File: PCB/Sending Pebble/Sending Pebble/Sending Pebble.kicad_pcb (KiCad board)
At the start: 4 copper layers, 50 x 72 mm, 46 parts, among them J1 USB_C_Receptacle_USB2.0_16P, J2 Conn_01x02_Socket, J3 u.Fl, J4 SMA, J5 Conn_01x02_Socket, Q1 IRLML0030, SW1 Boot, SW2 Reset, U1 LoRa-E5, U3 MAX-M10S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

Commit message: Power Circuitry almost finished
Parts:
- added R15: 10k, Resistor_SMD:R_0603_1608Metric, F.Cu at (28.8, 62.7)
- added R16: 36k, Resistor_SMD:R_0603_1608Metric, F.Cu at (28.8, 65.2)
- R10: value 3k -> 1.27k
- R9: value 3k -> 1.1k
- moved C3 112.0 mm to (133.6, 96.1)
- moved R8 105.4 mm to (137.8, 96.7), turned to 90 degrees
- moved R7 105.1 mm to (136.2, 96.7), turned to 90 degrees
- moved R9 97.4 mm to (132.2, 92.5), turned to -90 degrees
- moved R3 96.7 mm to (124.9, 88.9), turned to 180 degrees
- moved R10 96.0 mm to (125.7, 92.4)
- moved R2 95.8 mm to (125.7, 94.0), turned to 180 degrees
- moved U5 83.2 mm to (136.9, 89.9), turned to 90 degrees
- moved J5 71.6 mm to (144.4, 93.1), turned to 180 degrees
- moved U7 70.2 mm to (129.5, 95.3)
- moved J2 70.2 mm to (121.2, 98.8)
- moved R11 54.6 mm to (70.7, 87.8)
- moved R12 50.7 mm to (66.2, 87.9)
- moved D2 47.7 mm to (120.7, 82.0), turned to 180 degrees
- moved C11 22.8 mm to (61.9, 35.4)
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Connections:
- C3 pad 1: VBAT -> Net-(J5-Pin_2)
- C4 pad 1: Net-(J5-Pin_1) -> +3.3V
- J2 pad 1: Net-(J2-Pin_1) -> GND
- J2 pad 2: GND -> Net-(J2-Pin_2)
- J5 pad 1: Net-(J5-Pin_1) -> VBAT
- J5 pad 2: +3.3V -> Net-(J5-Pin_2)
- R10 pad 1: unconnected-(R10-Pad1) -> GND
- R9 pad 1: unconnected-(R9-Pad1) -> GND
- U1 pad 26: unconnected-(U1-PB14-Pad26) -> ADC
- U5 pad 1: VBAT -> Net-(J5-Pin_2)
- U5 pad 3: Net-(J5-Pin_1) -> +3.3V
- U7 pad 2: Net-(J2-Pin_1) -> Net-(J2-Pin_2)
- U7 pad 3: Net-(J2-Pin_1) -> Net-(J2-Pin_2)
- U7 pad 5: GND -> VBUS
- U7 pad 6: VBUS -> GND
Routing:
- net VBUS: track 0.00 -> 17.1 mm
- net D-: track 0.00 -> 10.4 mm
- net D+: track 0.07 -> 10.3 mm
- net (no net): track 0.00 -> 5.25 mm
- net Net-(U7-ISET): track 0.00 -> 2.84 mm
- net Net-(J1-CC2): track 0.00 -> 2.54 mm
- net Net-(J1-CC1): track 0.00 -> 2.34 mm
- net VBAT: track 0.00 -> 2.09 mm
- net Net-(U7-TS): track 0.00 -> 1.80 mm
- net Net-(U7-ILIM): track 0.00 -> 1.69 mm
- added copper zone on F.Cu, net Net-(J2-Pin_2)
- added copper zone on F.Cu, net VBAT
- removed copper zone on In2.Cu, net +3.3V
- removed copper zone on F.Cu, net GND
- removed copper zone on In1.Cu, net GND

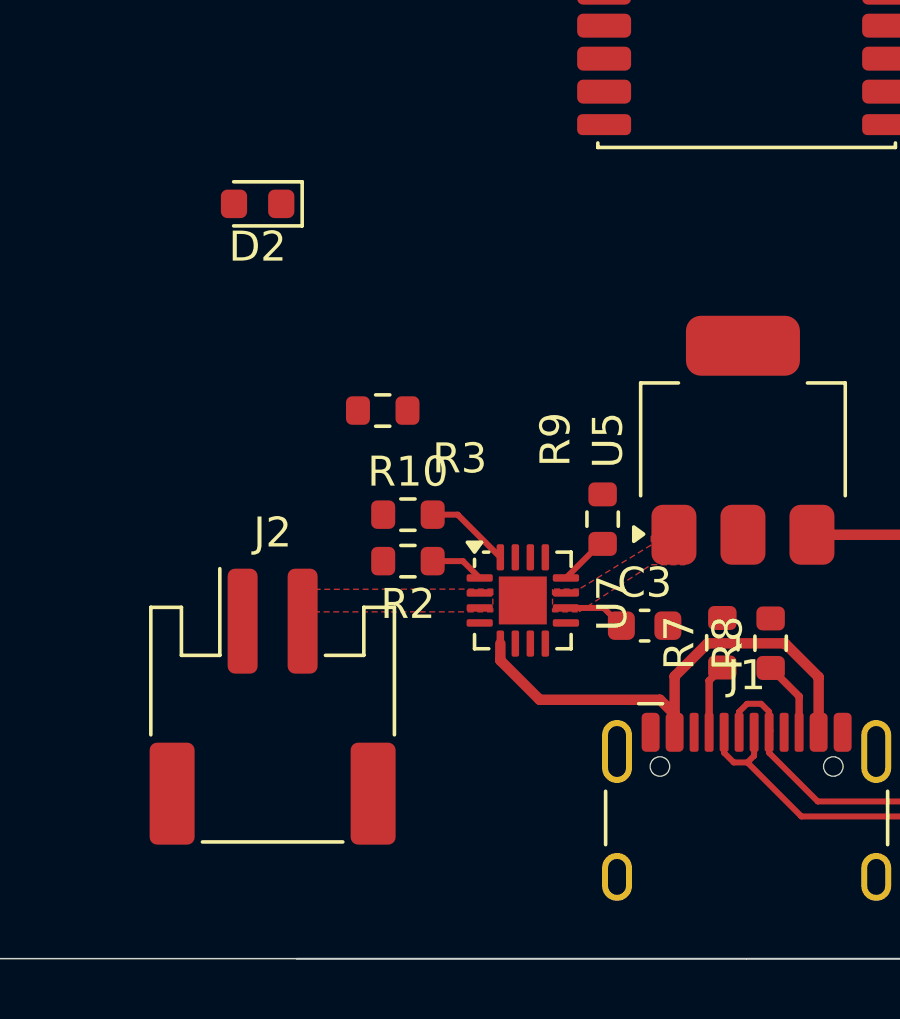
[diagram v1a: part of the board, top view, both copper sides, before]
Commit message: Updated DRC Rules
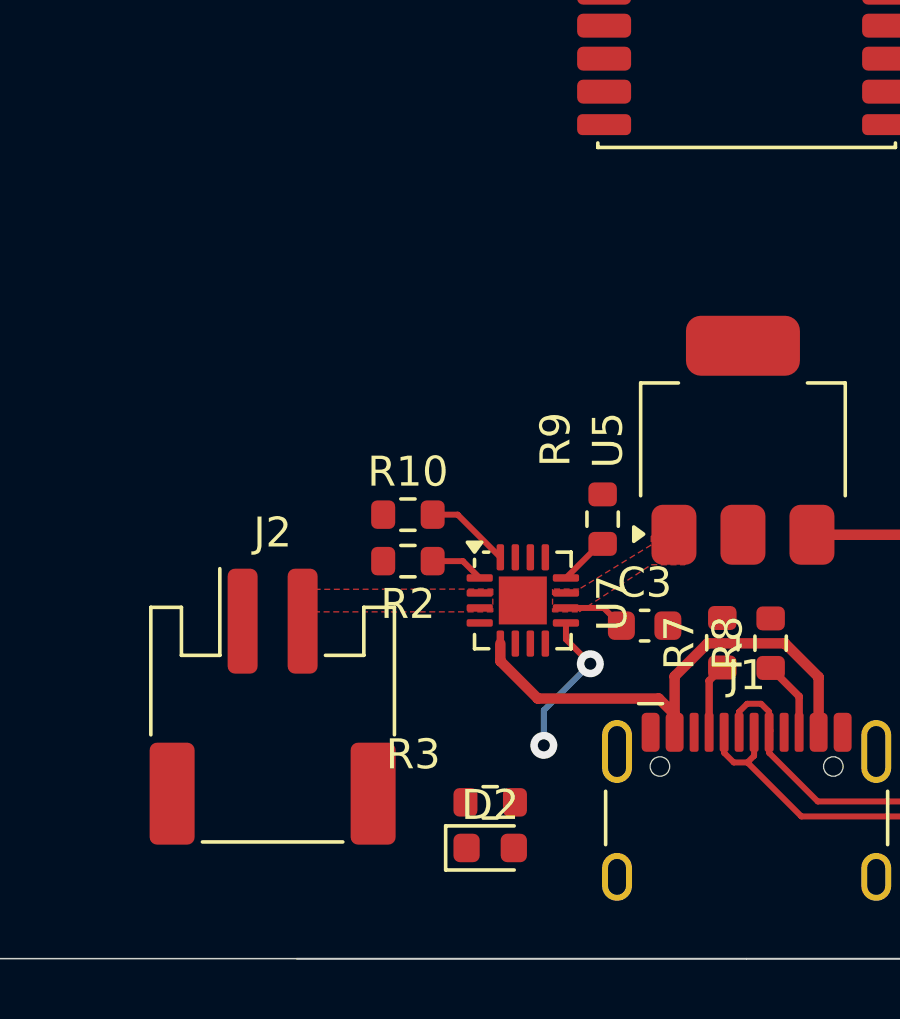
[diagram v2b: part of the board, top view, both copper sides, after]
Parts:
- moved D2 22.8 mm to (128.5, 103.5), turned to 0 degrees
- moved R3 13.5 mm to (128.5, 102.0), turned to 0 degrees
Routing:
- net Net-(U7-~{CHG}): track 0.00 -> 5.06 mm, vias 0 -> 2
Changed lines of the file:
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@@
 	(footprint "LED_SMD:LED_0603_1608Metric"
 		(layer "F.Cu")
-		(at 120.7 82.04 180)
+		(at 128.4525 103.51)
 		(descr "LED SMD 0603 (1608 Metric), square (rectangular) end terminal, IPC-7351 nominal, (Body size source: http://www.tortai-tech.com/upload/download/2011102023233369053.pdf), generated with kicad-footprint-generator")
 		(tags "LED")
@@
 		)
 		(property "Sim.Pins" "1=K 2=A"
-			(at 0 0 180)
+			(at 0 0 0)
 			(unlocked yes)
 			(layer "F.Fab")
@@
 		(attr smd)
 		(fp_line
-			(start 0.8 -0.735)
-			(end -1.485 -0.735)
+			(start -1.485 -0.735)
+			(end -1.485 0.735)
 			(stroke
 				(width 0.12)
@@
 		)
 		(fp_line
-			(start -1.485 -0.735)
-			(end -1.485 0.735)
+			(start 0.8 -0.735)
+			(end -1.485 -0.735)
 			(stroke
 				(width 0.12)
@@
 		)
 		(fp_line
-			(start 1.48 0.73)
-			(end -1.48 0.73)
+			(start -1.48 -0.73)
+			(end 1.48 -0.73)
 			(stroke
 				(width 0.05)
@@
 		)
 		(fp_line
-			(start 1.48 -0.73)
-			(end 1.48 0.73)
+			(start -1.48 0.73)
+			(end -1.48 -0.73)
 			(stroke
 				(width 0.05)
@@
 		)
 		(fp_line
-			(start -1.48 0.73)
-			(end -1.48 -0.73)
+			(start 1.48 -0.73)
+			(end 1.48 0.73)
 			(stroke
 				(width 0.05)
@@
 		)
 		(fp_line
-			(start -1.48 -0.73)
-			(end 1.48 -0.73)
+			(start 1.48 0.73)
+			(end -1.48 0.73)
 			(stroke
 				(width 0.05)
@@
 		)
 		(fp_line
-			(start 0.8 0.4)
-			(end 0.8 -0.4)
+			(start -0.8 -0.1)
+			(end -0.8 0.4)
 			(stroke
 				(width 0.1)
@@
 		)
 		(fp_line
-			(start 0.8 -0.4)
-			(end -0.5 -0.4)
+			(start -0.8 0.4)
+			(end 0.8 0.4)
 			(stroke
 				(width 0.1)
@@
 		)
 		(fp_line
-			(start -0.8 0.4)
-			(end 0.8 0.4)
+			(start 0.8 -0.4)
+			(end -0.5 -0.4)
 			(stroke
 				(width 0.1)
@@
 		)
 		(fp_line
-			(start -0.8 -0.1)
-			(end -0.8 0.4)
+			(start 0.8 0.4)
+			(end 0.8 -0.4)
 			(stroke
 				(width 0.1)
@@
 		)
 		(pad "1" smd roundrect
-			(at -0.7875 0 180)
+			(at -0.7875 0)
 			(size 0.875 0.95)
 			(layers "F.Cu" "F.Mask" "F.Paste")
@@
 		)
 		(pad "2" smd roundrect
-			(at 0.7875 0 180)
+			(at 0.7875 0)
 			(size 0.875 0.95)
 			(layers "F.Cu" "F.Mask" "F.Paste")
@@
 	(footprint "Resistor_SMD:R_0603_1608Metric"
 		(layer "F.Cu")
-		(at 124.87 88.93 180)
+		(at 128.4525 101.99)
 		(descr "Resistor SMD 0603 (1608 Metric), square (rectangular) end terminal, IPC-7351 nominal, (Body size source: IPC-SM-782 page 72, https://www.pcb-3d.com/wordpress/wp-content/uploads/ipc-sm-782a_amendment_1_and_2.pdf), generated with kicad-footprint-generator")
 		(tags "resistor")
@@
 		(attr smd)
 		(fp_line
-			(start -0.237258 0.5225)
-			(end 0.237258 0.5225)
+			(start -0.237258 -0.5225)
+			(end 0.237258 -0.5225)
 			(stroke
 				(width 0.12)
@@
 		)
 		(fp_line
-			(start -0.237258 -0.5225)
-			(end 0.237258 -0.5225)
+			(start -0.237258 0.5225)
+			(end 0.237258 0.5225)
 			(stroke
 				(width 0.12)
@@
 		)
 		(fp_line
-			(start 1.48 0.73)
-			(end -1.48 0.73)
+			(start -1.48 -0.73)
+			(end 1.48 -0.73)
 			(stroke
 				(width 0.05)
@@
 		)
 		(fp_line
-			(start 1.48 -0.73)
-			(end 1.48 0.73)
+			(start -1.48 0.73)
+			(end -1.48 -0.73)
 			(stroke
 				(width 0.05)
@@
 		)
 		(fp_line
-			(start -1.48 0.73)
-			(end -1.48 -0.73)
+			(start 1.48 -0.73)
+			(end 1.48 0.73)
 			(stroke
 				(width 0.05)
@@
 		)
 		(fp_line
-			(start -1.48 -0.73)
-			(end 1.48 -0.73)
+			(start 1.48 0.73)
+			(end -1.48 0.73)
 			(stroke
 				(width 0.05)
@@
 		)
 		(fp_line
-			(start 0.8 0.4125)
-			(end -0.8 0.4125)
+			(start -0.8 -0.4125)
+			(end 0.8 -0.4125)
 			(stroke
 				(width 0.1)
@@
 		)
 		(fp_line
-			(start 0.8 -0.4125)
-			(end 0.8 0.4125)
+			(start -0.8 0.4125)
+			(end -0.8 -0.4125)
 			(stroke
 				(width 0.1)
@@
 		)
 		(fp_line
-			(start -0.8 0.4125)
-			(end -0.8 -0.4125)
+			(start 0.8 -0.4125)
+			(end 0.8 0.4125)
 			(stroke
 				(width 0.1)
@@
 		)
 		(fp_line
-			(start -0.8 -0.4125)
-			(end 0.8 -0.4125)
+			(start 0.8 0.4125)
+			(end -0.8 0.4125)
 			(stroke
 				(width 0.1)
@@
 		)
 		(pad "1" smd roundrect
-			(at -0.825 0 180)
+			(at -0.825 0)
 			(size 0.8 0.95)
 			(layers "F.Cu" "F.Mask" "F.Paste")
@@
 		)
 		(pad "2" smd roundrect
-			(at 0.825 0 180)
+			(at 0.825 0)
 			(size 0.8 0.95)
 			(layers "F.Cu" "F.Mask" "F.Paste")
@@
 	)
 	(segment
-		(start 134.113034 98.57)
-		(end 130.103136 98.57)
-		(width 0.35)
-		(layer "F.Cu")
-		(net 6)
-	)
-	(segment
-		(start 134.6 99.056966)
-		(end 134.113034 98.57)
+		(start 130.04 98.53)
+		(end 128.79 97.28)
 		(width 0.35)
 		(layer "F.Cu")
@@
 	)
 	(segment
-		(start 128.79 97.256864)
-		(end 128.79 96.6975)
+		(start 134.073034 98.53)
+		(end 130.04 98.53)
 		(width 0.35)
 		(layer "F.Cu")
@@
 	)
 	(segment
-		(start 130.103136 98.57)
-		(end 128.79 97.256864)
+		(start 134.6 99.056966)
+		(end 134.073034 98.53)
 		(width 0.35)
 		(layer "F.Cu")
@@
 	)
 	(segment
-		(start 138.27513 96.69)
-		(end 139.4 97.81487)
+		(start 128.79 97.28)
+		(end 128.79 96.6975)
 		(width 0.35)
 		(layer "F.Cu")
@@
 	)
 	(segment
-		(start 134.6 99.655)
-		(end 134.6 99.056966)
+		(start 138.27513 96.69)
+		(end 139.4 97.81487)
 		(width 0.35)
 		(layer "F.Cu")
@@
 	)
 	(segment
+		(start 134.6 99.655)
+		(end 134.6 99.056966)
+		(width 0.35)
+		(layer "F.Cu")
+		(net 6)
+	)
+	(segment
 		(start 137.75 99.655)
 		(end 137.75 100.338824)
@@
 	)
 	(segment
+		(start 130.9775 96.01)
+		(end 130.9775 96.5575)
+		(width 0.2)
+		(layer "F.Cu")
+		(net 24)
+	)
+	(segment
+		(start 130.9775 96.5575)
+		(end 131.79 97.37)
+		(width 0.2)
+		(layer "F.Cu")
+		(net 24)
+	)
+	(via
+		(at 131.79 97.37)
+		(size 0.9)
+		(drill 0.4)
+		(layers "F.Cu" "B.Cu")
+		(free yes)
+		(net 24)
+	)
+	(via
+		(at 130.24 100.09)
+		(size 0.9)
+		(drill 0.4)
+		(layers "F.Cu" "B.Cu")
+		(free yes)
+		(net 24)
+	)
+	(segment
+		(start 130.24 100.09)
+		(end 130.24 98.92)
+		(width 0.2)
+		(layer "B.Cu")
+		(net 24)
+	)
+	(segment
+		(start 130.24 98.92)
+		(end 131.79 97.37)
+		(width 0.2)
+		(layer "B.Cu")
+		(net 24)
+	)
+	(segment

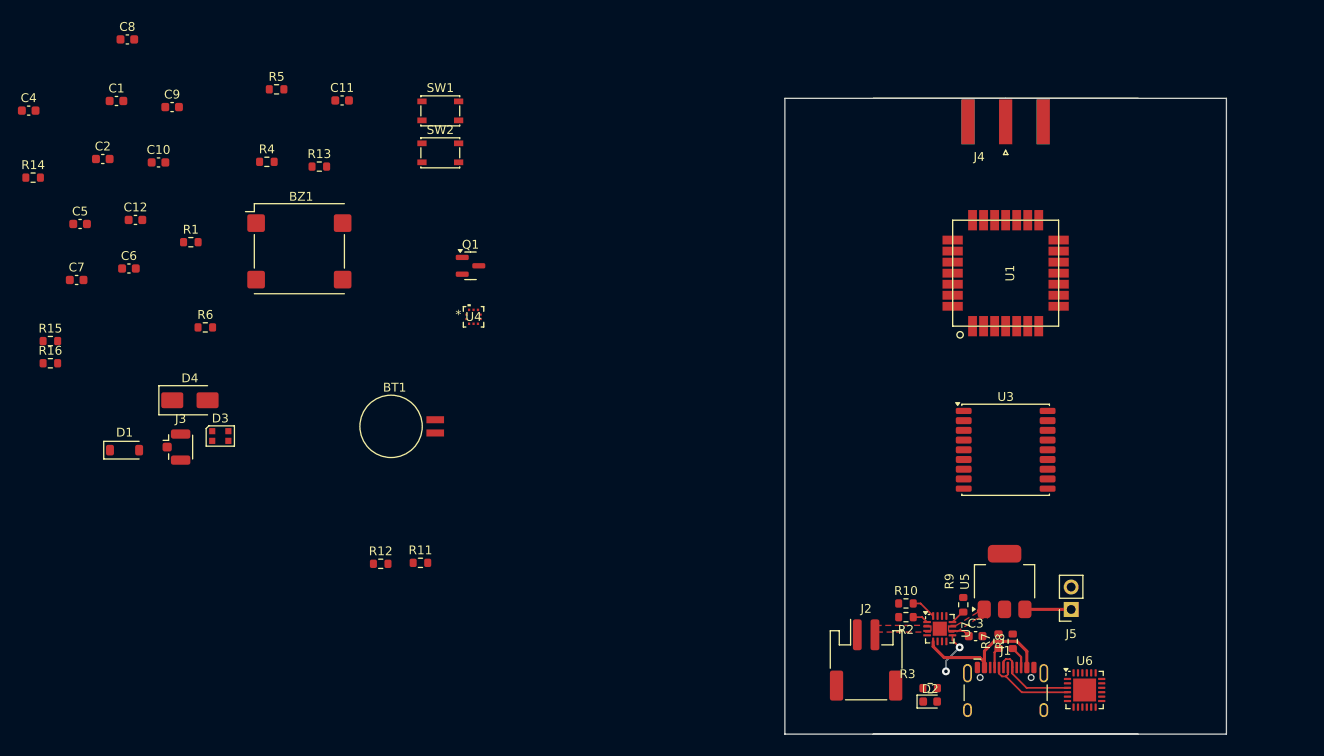
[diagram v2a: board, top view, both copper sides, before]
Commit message: Finalized form factor, added coplanar waveguides for feedlines and placed all components on board
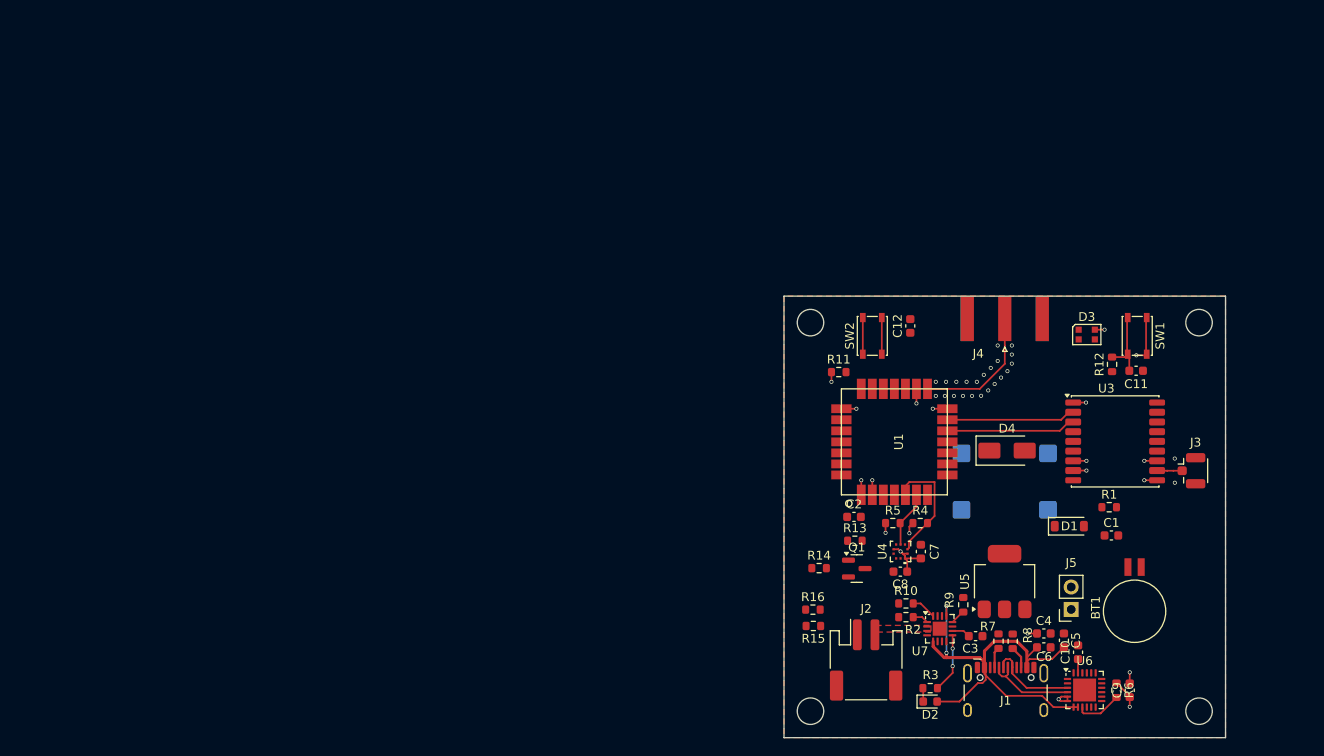
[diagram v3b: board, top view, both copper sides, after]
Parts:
- BZ1: moved to B.Cu
- moved C4 129.3 mm to (141.3, 95.8)
- moved C9 127.0 mm to (151.1, 102.2), turned to 90 degrees
- moved C1 122.9 mm to (149.0, 84.7)
- moved C5 121.0 mm to (143.6, 96.6), turned to 90 degrees
- moved C10 118.0 mm to (145.2, 97.9), turned to 90 degrees
- moved J3 115.0 mm to (158.0, 77.4)
- moved C6 112.1 mm to (141.3, 97.4)
- moved R6 111.1 mm to (149.6, 102.2), turned to -90 degrees
- moved R1 108.2 mm to (148.7, 81.5)
- moved D1 107.3 mm to (144.2, 83.7)
- moved C8 106.3 mm to (125.1, 88.8), turned to 180 degrees
- moved C7 100.4 mm to (127.4, 86.5), turned to 90 degrees
- moved R14 99.4 mm to (115.9, 88.4)
- moved D3 98.8 mm to (146.2, 62.0)
- moved C11 95.0 mm to (151.8, 66.0), turned to 180 degrees
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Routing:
- net VBUS: track 17.2 -> 53.3 mm, vias 0 -> 2
- net +3.3V: track 0.00 -> 27.8 mm, vias 0 -> 12
- net GND: track 0.00 -> 16.4 mm, vias 0 -> 32
- net Net-(J4-In): track 0.00 -> 15.0 mm
- net TXD: track 0.00 -> 14.7 mm
- net RXD: track 0.00 -> 14.6 mm
- net SCL: track 0.00 -> 13.4 mm
- net BOOT0: track 0.00 -> 7.91 mm
- net SDA: track 0.00 -> 6.41 mm
- net (no net): track 5.25 -> 0.00 mm
- net Net-(U6-~{RST}): track 0.00 -> 5.24 mm
- net RST: track 0.00 -> 4.15 mm
- net Net-(J3-In): track 0.00 -> 2.88 mm
- net Net-(U7-~{CHG}): track 5.06 -> 6.70 mm
- net Net-(U6-~{DTR}): track 0.00 -> 1.57 mm
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- added copper zone on In2.Cu, net +3.3V
- added copper zone on F.Cu, net GND
- added copper zone on In1.Cu, net GND
- removed copper zone on F.Cu, net VBAT
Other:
- board size 50 x 72 mm -> 50 x 50 mm
